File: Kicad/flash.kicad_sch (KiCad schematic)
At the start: 5 parts, among them U13 SST39SF010/020/040, U14 W25X40CLSN

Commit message: Recreate PCB from schematics
Changed footprints to sync cleanly on the Mac
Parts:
- C1401: footprint kicad-official/Capacitor_SMD.pretty:C_0603_1608Metric_Pad1.08x0.95mm_HandSolder -> Capacitor_SMD:C_0603_1608Metric_Pad1.08x0.95mm_HandSolder
- R13, R1401: footprint kicad-official/Resistor_SMD.pretty:R_0603_1608Metric -> Resistor_SMD:R_0603_1608Metric_Pad0.98x0.95mm_HandSolder
- U13: footprint kicad-official/Package_SO.pretty:TSOP-I-32_11.8x8mm_P0.5mm -> Package_SO:TSOP-I-32_11.8x8mm_P0.5mm
- U14: footprint kicad-official/Package_SO.pretty:SOIC-8_3.9x4.9mm_P1.27mm -> Package_SO:SOIC-8_3.9x4.9mm_P1.27mm
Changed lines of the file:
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@@
 			)
 		)
-		(property "Footprint" "kicad-official/Package_SO.pretty:TSOP-I-32_11.8x8mm_P0.5mm"
+		(property "Footprint" "Package_SO:TSOP-I-32_11.8x8mm_P0.5mm"
 			(at 63.5 58.42 0)
 			(effects
@@
 			)
 		)
-		(property "Footprint" "kicad-official/Package_SO.pretty:SOIC-8_3.9x4.9mm_P1.27mm"
+		(property "Footprint" "Package_SO:SOIC-8_3.9x4.9mm_P1.27mm"
 			(at 124.46 24.13 0)
 			(effects
@@
 			)
 		)
-		(property "Footprint" "kicad-official/Capacitor_SMD.pretty:C_0603_1608Metric_Pad1.08x0.95mm_HandSolder"
+		(property "Footprint" "Capacitor_SMD:C_0603_1608Metric_Pad1.08x0.95mm_HandSolder"
 			(at 143.51 35.56 0)
 			(effects
@@
 			)
 		)
-		(property "Footprint" "kicad-official/Resistor_SMD.pretty:R_0603_1608Metric"
+		(property "Footprint" "Resistor_SMD:R_0603_1608Metric_Pad0.98x0.95mm_HandSolder"
 			(at 109.22 35.56 0)
 			(effects
@@
 			)
 		)
-		(property "Footprint" "kicad-official/Resistor_SMD.pretty:R_0603_1608Metric"
+		(property "Footprint" "Resistor_SMD:R_0603_1608Metric_Pad0.98x0.95mm_HandSolder"
 			(at 35.56 96.52 0)
 			(effects

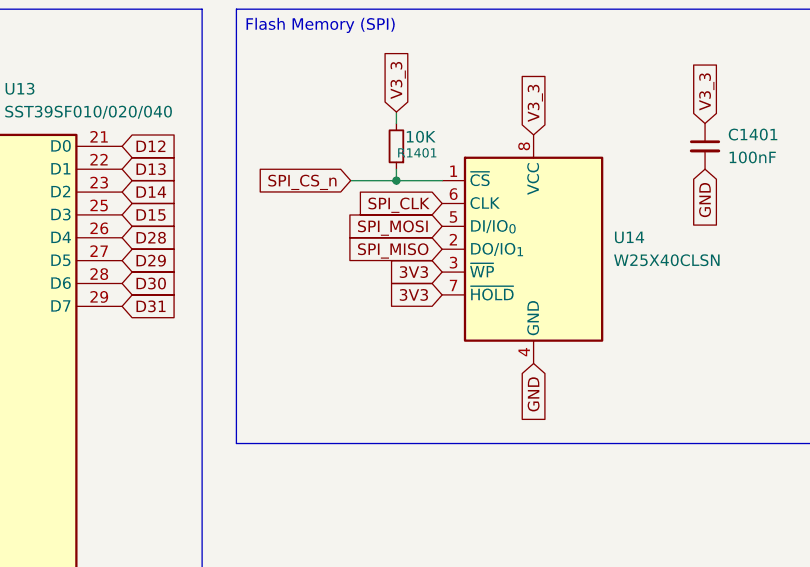
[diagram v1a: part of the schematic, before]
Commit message: Fix 3V3 -> V3_3
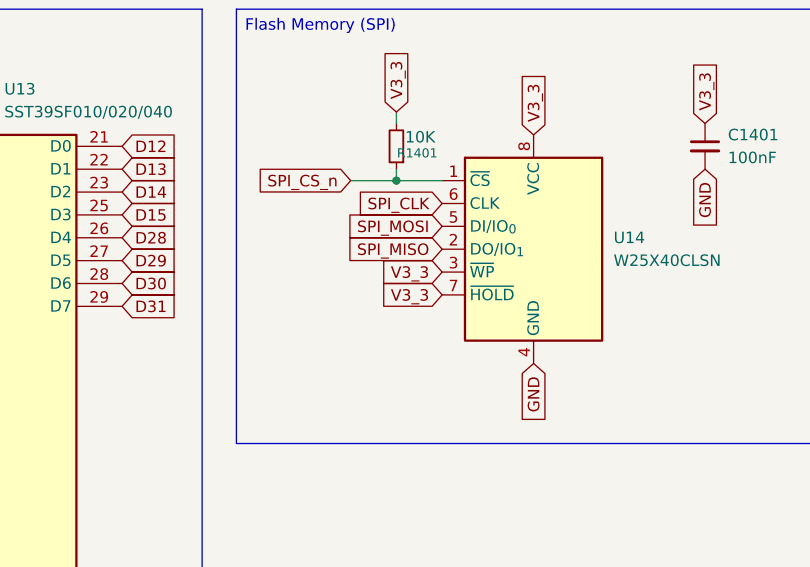
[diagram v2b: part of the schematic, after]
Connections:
- net 3V3 is gone; now on net V3_3: U14.3 (~{WP}), U14.7 (~{HOLD})
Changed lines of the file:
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@@
 		)
 	)
-	(global_label "3V3"
+	(global_label "V3_3"
 		(shape input)
 		(at 114.3 52.07 180)
@@
 		)
 		(property "Intersheetrefs" "${INTERSHEET_REFS}"
-			(at 107.8072 52.07 0)
+			(at 106.8396 52.07 0)
 			(effects
 				(font
@@
 		)
 	)
-	(global_label "3V3"
+	(global_label "V3_3"
 		(shape input)
 		(at 114.3 49.53 180)
@@
 		)
 		(property "Intersheetrefs" "${INTERSHEET_REFS}"
-			(at 107.8072 49.53 0)
-			(effects
-				(font
+			(at 106.8396 49.53 0)
+			(effects
+				(font
